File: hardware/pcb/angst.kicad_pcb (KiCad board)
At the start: 2 copper layers, 50.8 x 50.8 mm, 90 parts, among them J1 USB_B_Micro, J2 Conn_02x05_Odd_Even, J3 Conn_01x02_Male, J4 Conn_01x03, J5 Conn_01x03, J6 Conn_01x03, J7 Conn_01x02_Male, J8 Conn_01x04_Male, J9 Conn_01x02_Male, Q1 IRLML6401TRPBF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

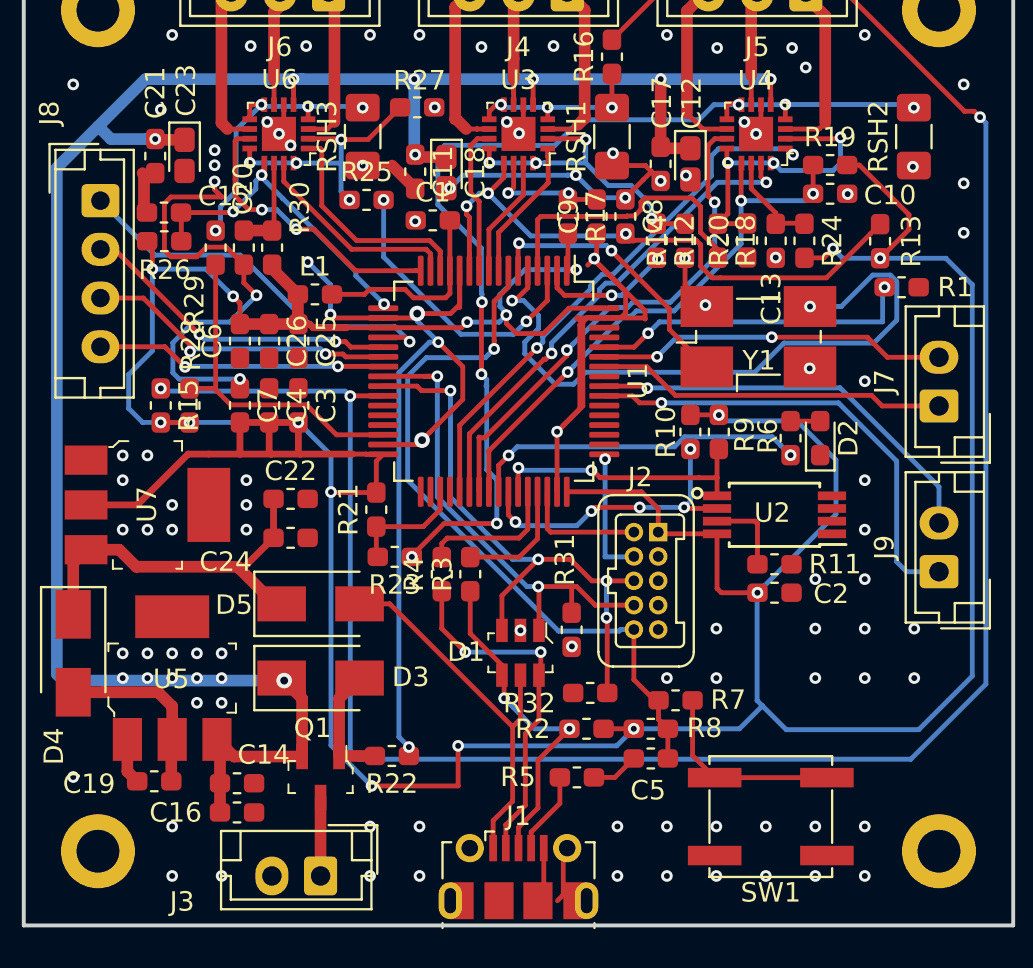
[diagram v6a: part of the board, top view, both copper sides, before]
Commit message: Finish layout and board art. V1.0 production ready
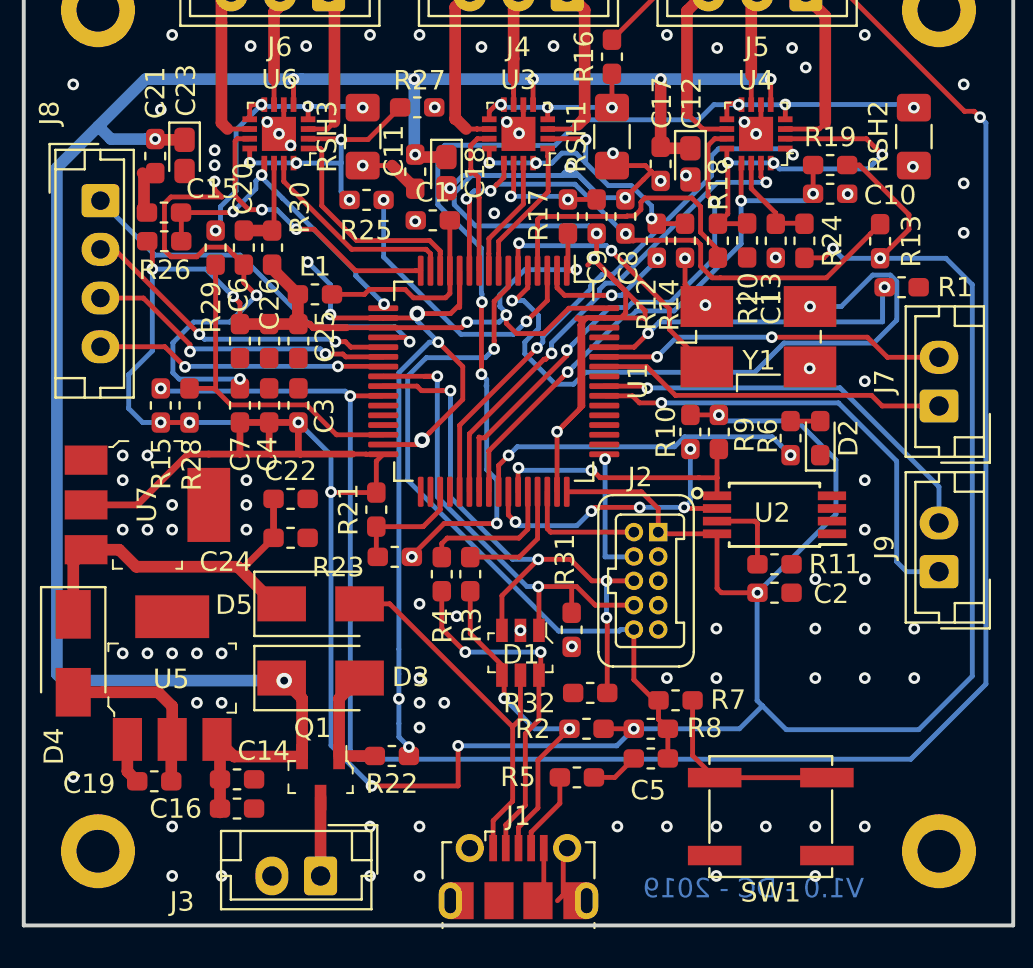
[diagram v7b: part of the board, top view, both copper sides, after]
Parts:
- moved C14 0.20 mm to (125.2, 81.4)
- moved C16 0.20 mm to (125.2, 82.9)
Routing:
- net GND: track 138.7 -> 155.9 mm, vias 110 -> 115
- net Net-(R18-Pad1): track 15.9 -> 19.3 mm
- net PC3: track 31.0 -> 31.5 mm
- net +BATT: vias 13 -> 8
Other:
- board text added: "A.N.G.S.T."
- board text added: "V1.0 - DC - 2019"
